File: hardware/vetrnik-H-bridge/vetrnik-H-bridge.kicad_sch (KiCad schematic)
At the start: 58 parts, among them J1 Conn_01x05, J2 Conn_01x02_Pin, J3 Conn_01x02_Pin, J4 Conn_01x02_Pin, J5 Conn_01x02_Pin, U1 IR2104, U2 IR2104

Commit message: [hardware] Exclude vetrnik-H-bridge parts from BOM
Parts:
- D12, D13, D14, D15, H1, H2, H3, H4: now left out of the parts list
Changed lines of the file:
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@@
   )
   (symbol (lib_id "Mechanical:MountingHole") (at 50.8 190.5 0) (unit 1)
-    (in_bom yes) (on_board yes) (dnp no) (fields_autoplaced)
+    (in_bom no) (on_board yes) (dnp no) (fields_autoplaced)
     (property "Reference" "H4" (at 53.34 189.2879 0)
       (effects (font (size 1.27 1.27)) (justify left))
@@
   )
   (symbol (lib_id "Diode:1N4148W") (at 234.95 97.79 0) (unit 1)
-    (in_bom yes) (on_board yes) (dnp yes)
+    (in_bom no) (on_board yes) (dnp yes)
     (property "Reference" "D15" (at 243.84 97.79 0)
       (effects (font (size 1.27 1.27)))
@@
   )
   (symbol (lib_id "Mechanical:MountingHole") (at 25.4 190.5 0) (unit 1)
-    (in_bom yes) (on_board yes) (dnp no) (fields_autoplaced)
+    (in_bom no) (on_board yes) (dnp no) (fields_autoplaced)
     (property "Reference" "H2" (at 27.94 189.2879 0)
       (effects (font (size 1.27 1.27)) (justify left))
@@
   )
   (symbol (lib_id "Diode:1N4148W") (at 234.95 76.2 0) (unit 1)
-    (in_bom yes) (on_board yes) (dnp yes)
+    (in_bom no) (on_board yes) (dnp yes)
     (property "Reference" "D14" (at 243.84 73.66 0)
       (effects (font (size 1.27 1.27)))
@@
   )
   (symbol (lib_id "Diode:1N4148W") (at 234.95 25.4 0) (unit 1)
-    (in_bom yes) (on_board yes) (dnp yes)
+    (in_bom no) (on_board yes) (dnp yes)
     (property "Reference" "D12" (at 243.84 22.86 0)
       (effects (font (size 1.27 1.27)))
@@
   )
   (symbol (lib_id "Diode:1N4148W") (at 234.95 46.99 0) (unit 1)
-    (in_bom yes) (on_board yes) (dnp yes)
+    (in_bom no) (on_board yes) (dnp yes)
     (property "Reference" "D13" (at 243.84 46.99 0)
       (effects (font (size 1.27 1.27)))
@@
   )
   (symbol (lib_id "Mechanical:MountingHole") (at 25.4 177.8 0) (unit 1)
-    (in_bom yes) (on_board yes) (dnp no) (fields_autoplaced)
+    (in_bom no) (on_board yes) (dnp no) (fields_autoplaced)
     (property "Reference" "H1" (at 27.94 176.5879 0)
       (effects (font (size 1.27 1.27)) (justify left))
@@
   )
   (symbol (lib_id "Mechanical:MountingHole") (at 50.8 177.8 0) (unit 1)
-    (in_bom yes) (on_board yes) (dnp no) (fields_autoplaced)
+    (in_bom no) (on_board yes) (dnp no) (fields_autoplaced)
     (property "Reference" "H3" (at 53.34 176.5879 0)
       (effects (font (size 1.27 1.27)) (justify left))

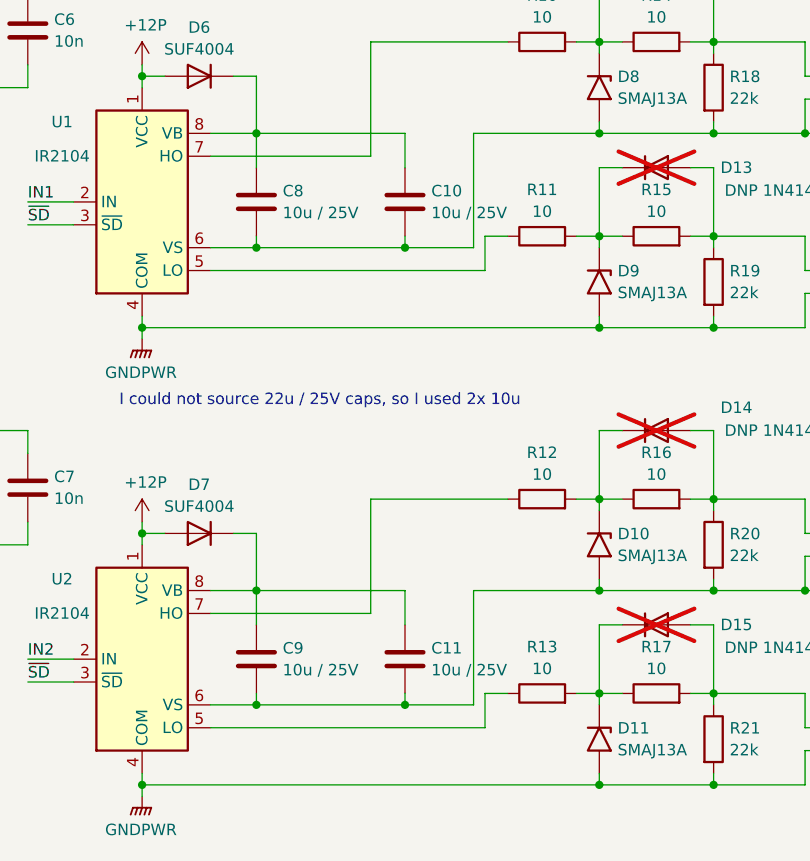
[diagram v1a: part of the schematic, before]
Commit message: [hardware] Add info about hardware mods
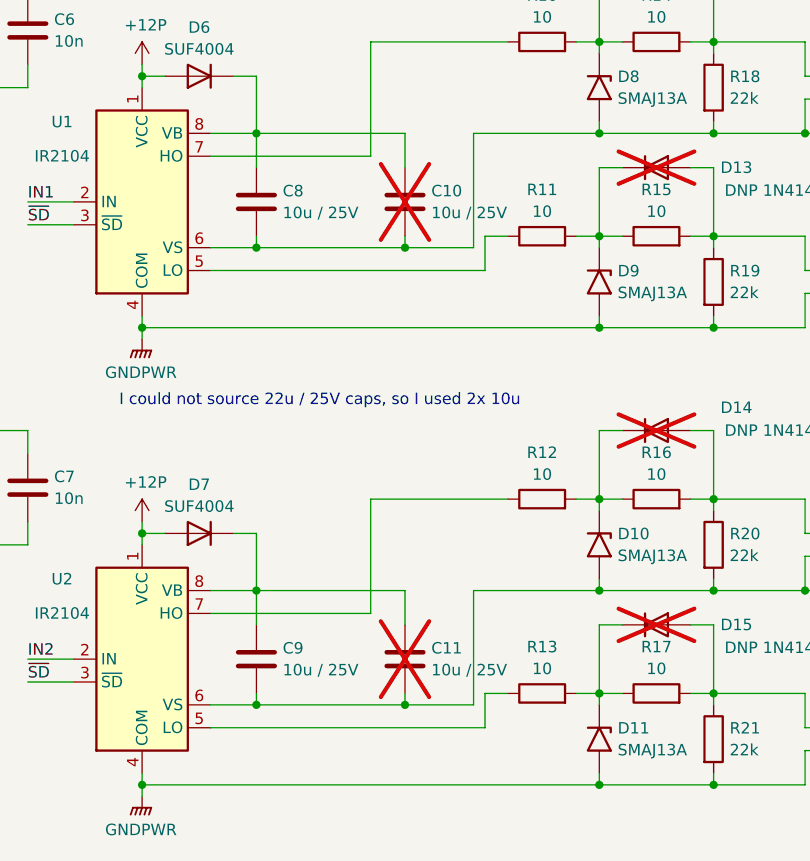
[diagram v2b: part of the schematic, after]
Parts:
- C10, C11: now not fitted
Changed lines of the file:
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@@
   )
   (symbol (lib_id "Device:C") (at 207.01 101.6 0) (unit 1)
-    (in_bom yes) (on_board yes) (dnp no) (fields_autoplaced)
+    (in_bom yes) (on_board yes) (dnp yes) (fields_autoplaced)
     (property "Reference" "C11" (at 209.931 100.3879 0)
       (effects (font (size 1.27 1.27)) (justify left))
@@
   )
   (symbol (lib_id "Device:C") (at 207.01 50.8 0) (unit 1)
-    (in_bom yes) (on_board yes) (dnp no)
+    (in_bom yes) (on_board yes) (dnp yes)
     (property "Reference" "C10" (at 209.931 49.5879 0)
       (effects (font (size 1.27 1.27)) (justify left))

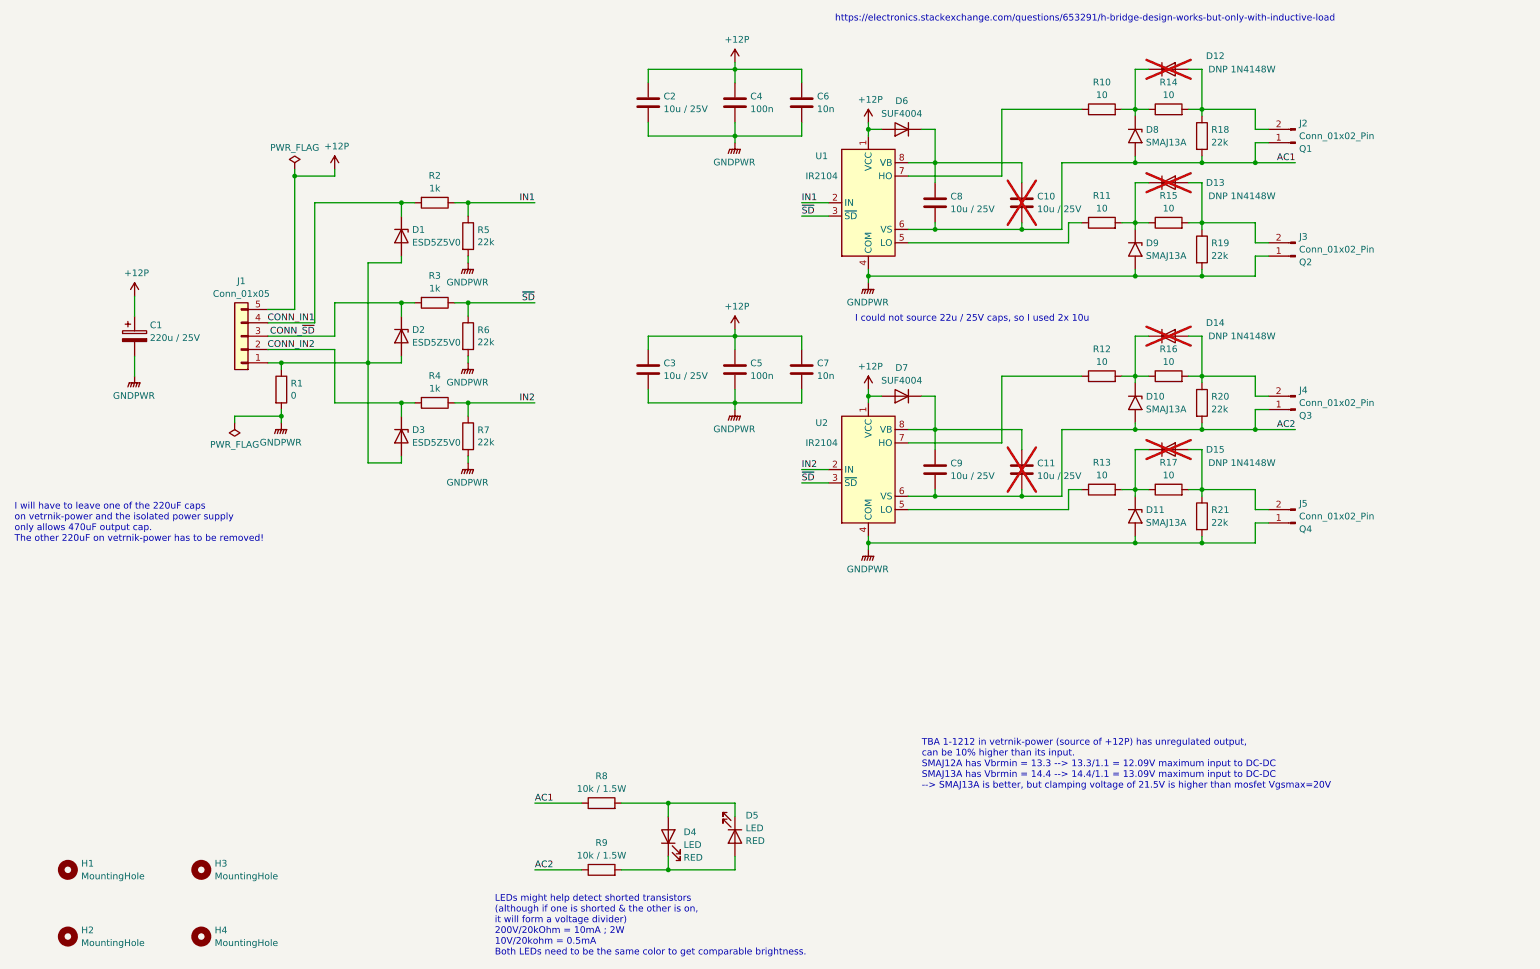
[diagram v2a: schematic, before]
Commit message: [hardware] Clean up vetrnik-H-bridge schematic
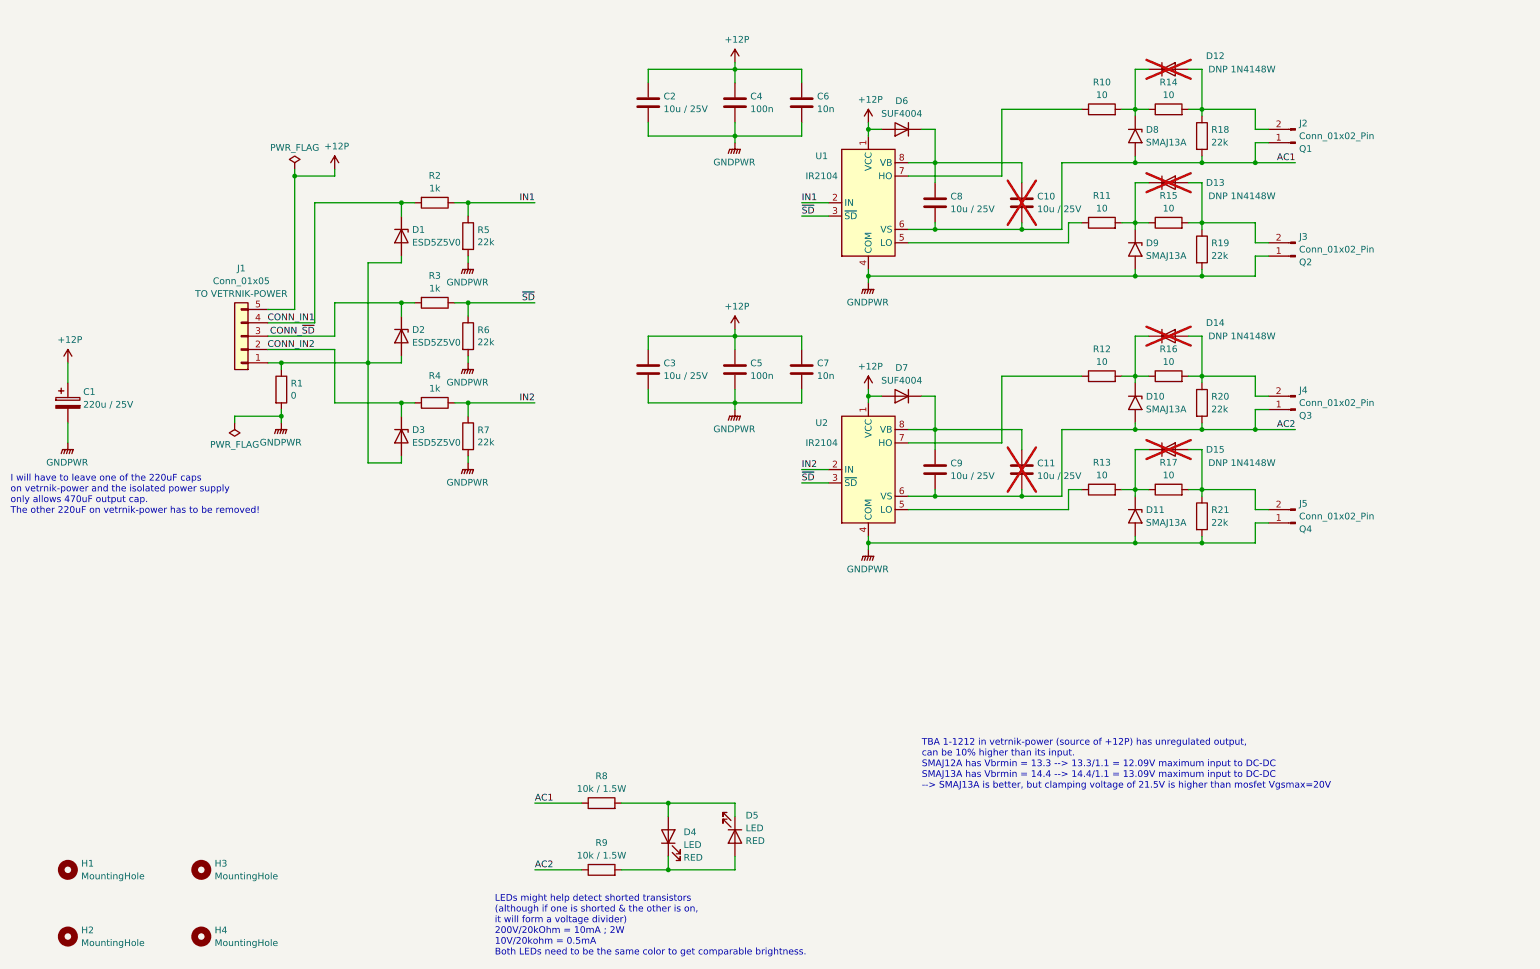
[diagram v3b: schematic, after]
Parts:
- J1: Label (none) -> TO VETRNIK-POWER
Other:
- note removed: "I could not source 22u / 25V caps, so I used 2x 10u"
- note removed: "https://electronics.stackexchange.com/questions/653291/h-bridge-design-works-but-only-with-inductive-load"
- moved on the sheet: C1
